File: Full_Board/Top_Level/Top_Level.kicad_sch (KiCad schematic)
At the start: 3 parts

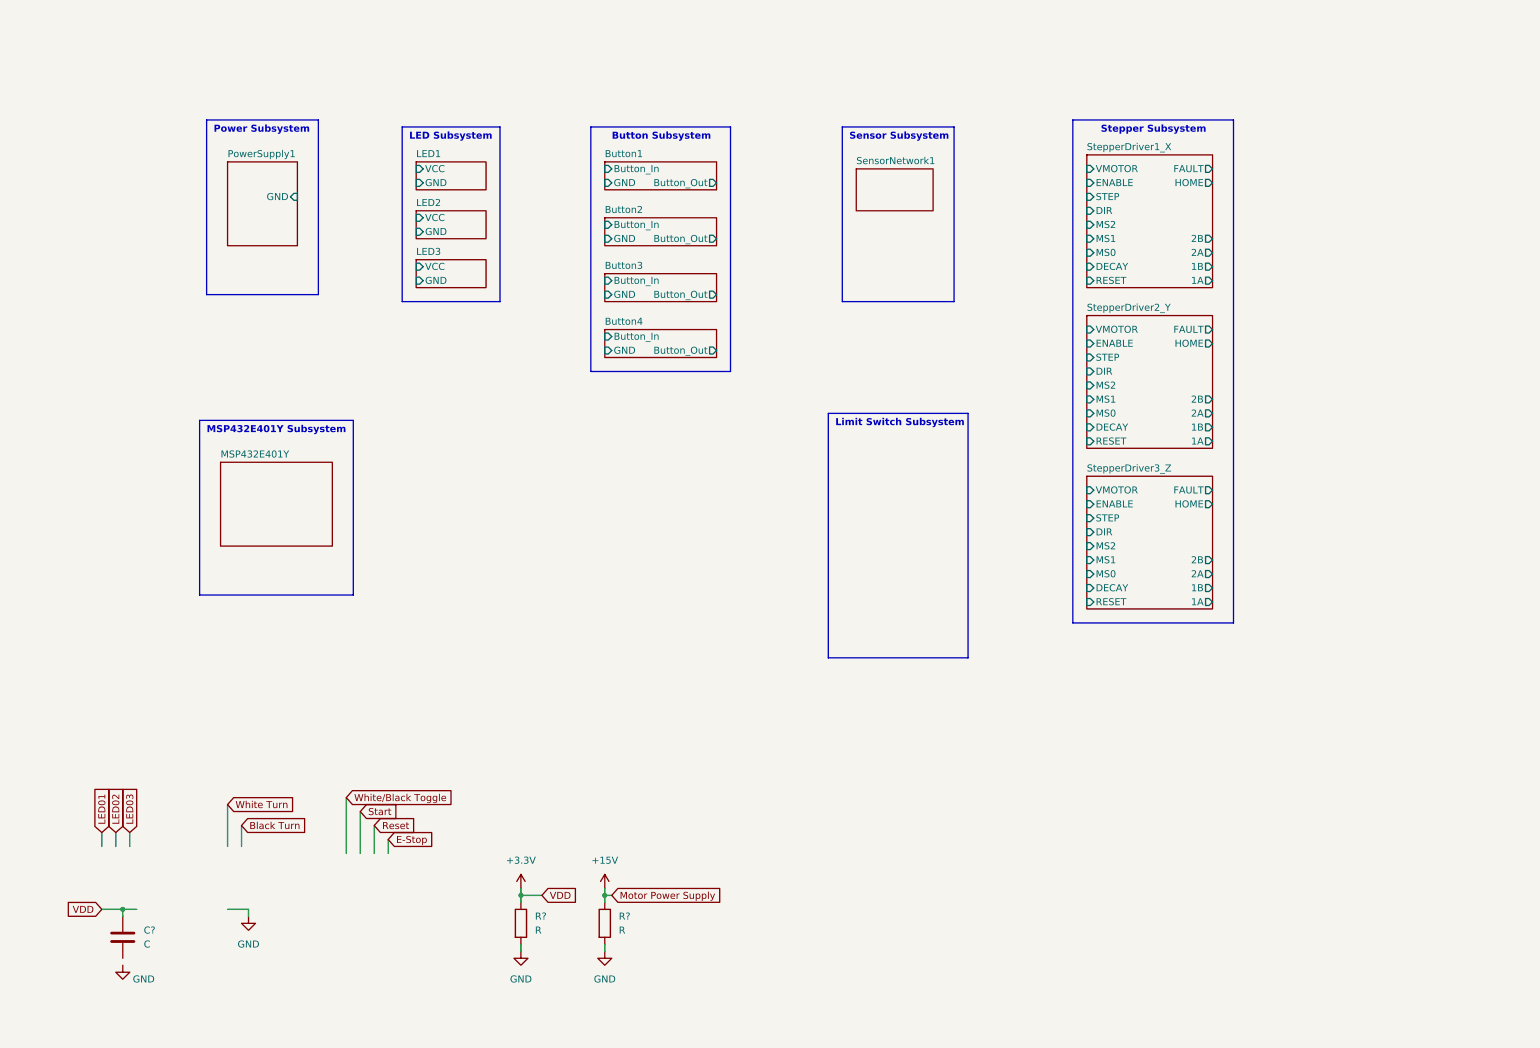
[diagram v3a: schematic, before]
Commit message: Finalize MSP432, stepper, and button subsheets
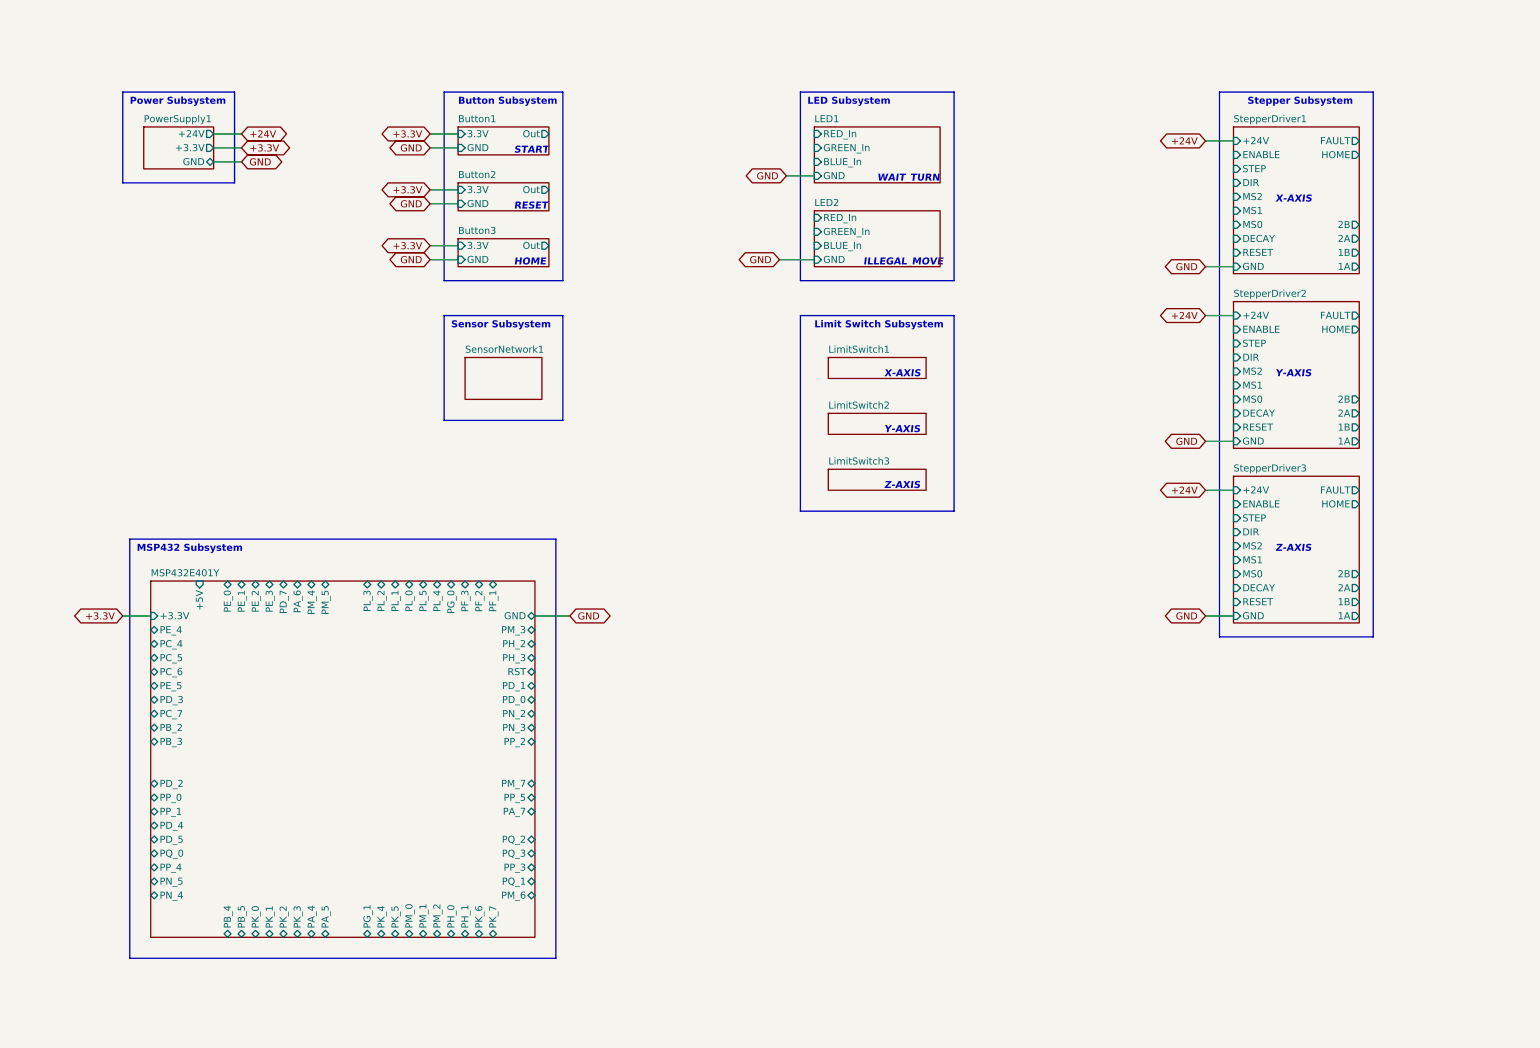
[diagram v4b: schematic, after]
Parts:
- removed C?: C, symbol Device:C
- removed R? (x2): R, symbol Device:R
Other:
- sheet StepperDriver1_X renamed StepperDriver1
- removed sheet Button4
- removed sheet LED3
- removed sheet StepperDriver2_Y
- removed sheet StepperDriver3_Z
- added sheet LimitSwitch1 (../Limit_Switch_Subsystem/LimitSwitch.kicad_sch)
- added sheet LimitSwitch2 (../Limit_Switch_Subsystem/LimitSwitch.kicad_sch)
- added sheet LimitSwitch3 (../Limit_Switch_Subsystem/LimitSwitch.kicad_sch)
- added sheet StepperDriver2 (../Stepper_Subsystem/Stepper_Driver.kicad_sch)
- added sheet StepperDriver3 (../Stepper_Subsystem/Stepper_Driver.kicad_sch)
- sheet Button1 ports: added 3.3V, Out; removed Button_In, Button_Out
- sheet Button2 ports: added 3.3V, Out; removed Button_In, Button_Out
- sheet Button3 ports: added 3.3V, Out; removed Button_In, Button_Out
- sheet LED1 ports: added BLUE_In, GREEN_In, RED_In; removed VCC
- sheet LED2 ports: added BLUE_In, GREEN_In, RED_In; removed VCC
- sheet MSP432E401Y ports: added +3.3V, +5V, GND, PA_4, PA_5, PA_6, PA_7, PB_2, PB_3, PB_4, PB_5, PC_4, PC_5, PC_6, PC_7, PD_0, PD_1, PD_2, PD_3, PD_4, PD_5, PD_7, PE_0, PE_1, PE_2, PE_3, PE_4, PE_5, PF_1, PF_2, PF_3, PG_0, PG_1, PH_0, PH_1, PH_2, PH_3, PK_0, PK_1, PK_2, PK_3, PK_4, PK_5, PK_6, PK_7, PL_0, PL_1, PL_2, PL_3, PL_4, PL_5, PM_0, PM_1, PM_2, PM_3, PM_4, PM_5, PM_6, PM_7, PN_2, PN_3, PN_4, PN_5, PP_0, PP_1, PP_2, PP_3, PP_4, PP_5, PQ_0, PQ_1, PQ_2, PQ_3, RST; removed none
- sheet PowerSupply1 ports: added +24V, +3.3V; removed none
- sheet StepperDriver1 ports: added +24V, GND; removed VMOTOR
- note added: "HOME"
- note added: "ILLEGAL_MOVE"
- note added: "MSP432 Subsystem"
- note added: "RESET"
- note added: "START"
- note added: "WAIT_TURN"
- note added: "X-AXIS"
- note added: "Y-AXIS"
- note added: "Z-AXIS"
- note removed: "MSP432E401Y Subsystem"

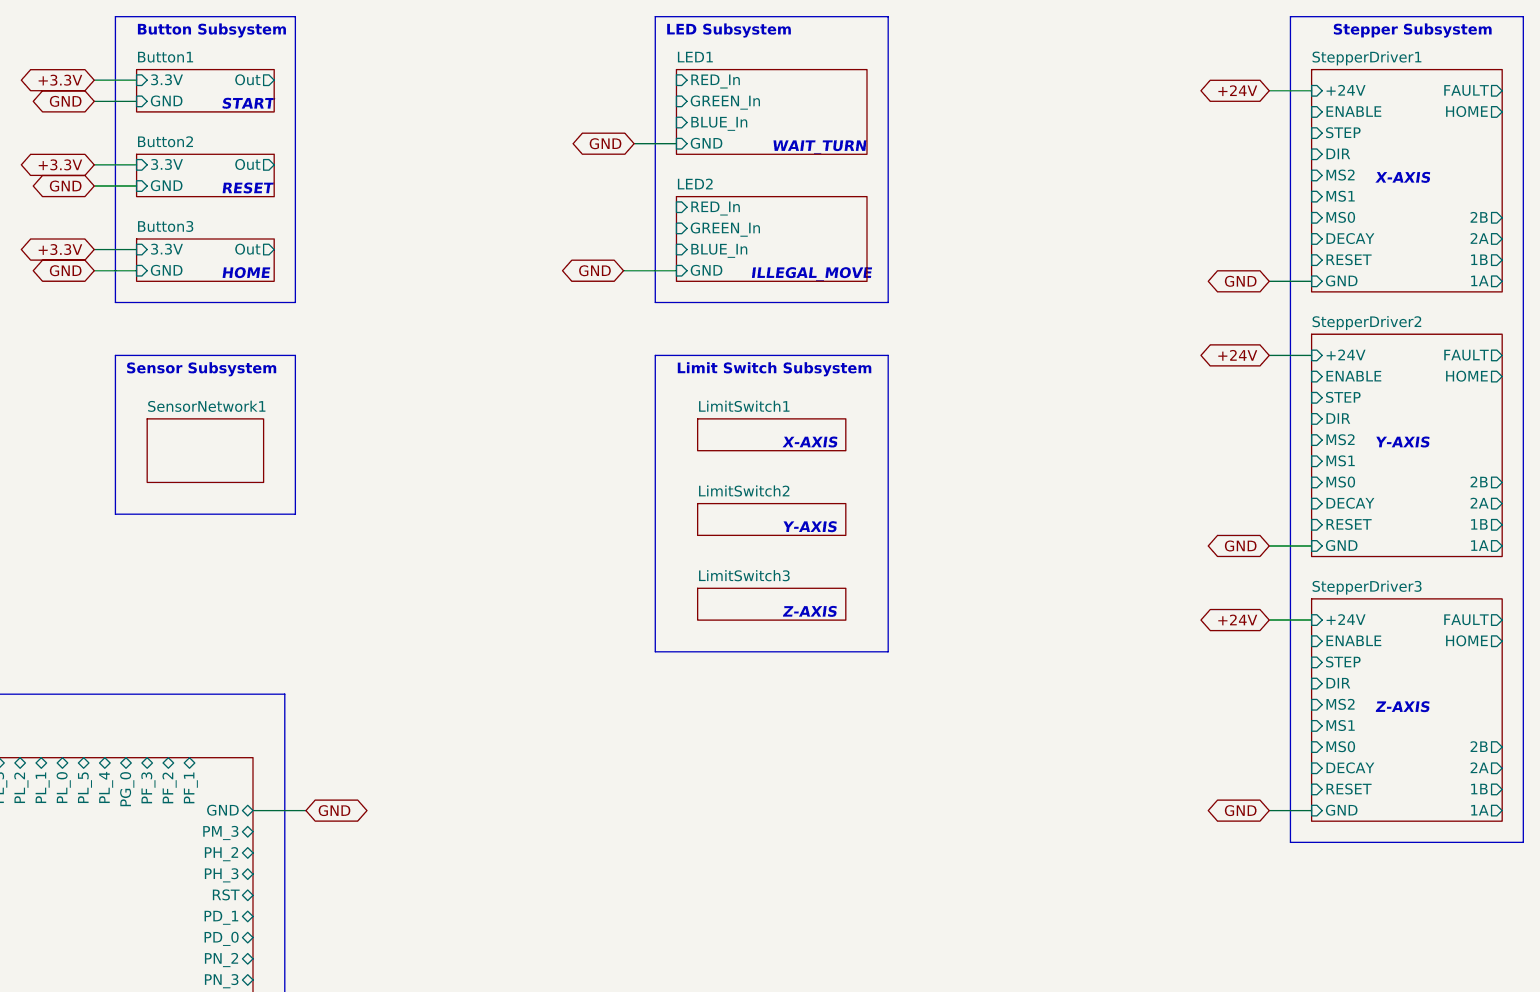
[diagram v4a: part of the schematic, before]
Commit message: Layout LED subsystem
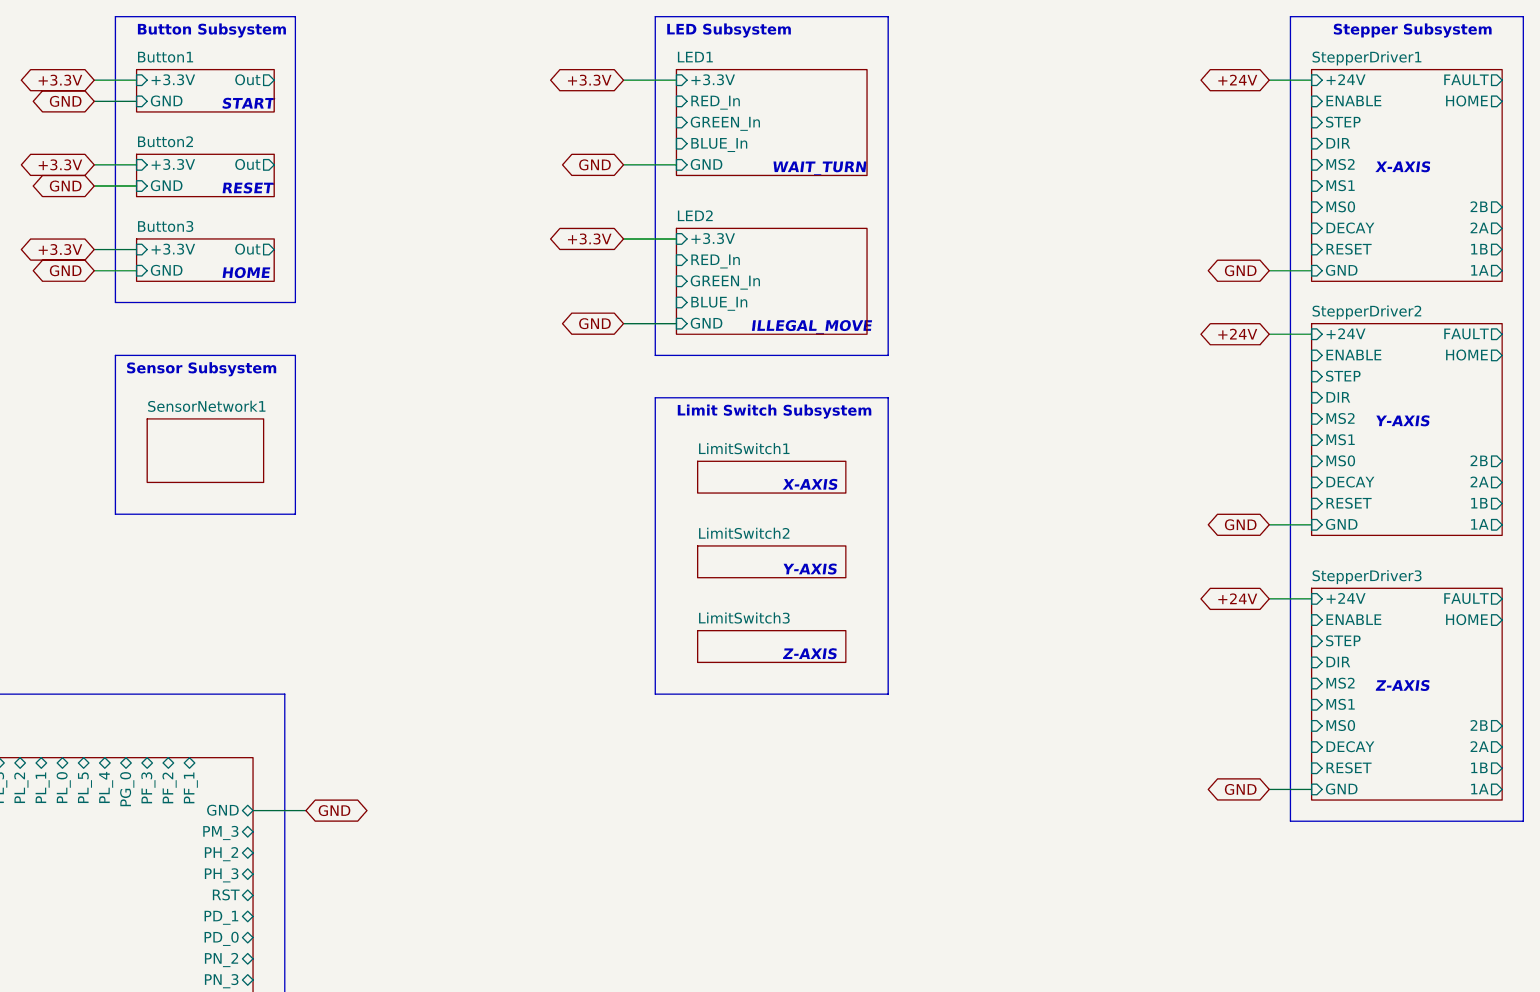
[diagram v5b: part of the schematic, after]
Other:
- sheet Button1 ports: added +3.3V; removed 3.3V
- sheet Button2 ports: added +3.3V; removed 3.3V
- sheet Button3 ports: added +3.3V; removed 3.3V
- sheet LED1 ports: added +3.3V; removed none
- sheet LED2 ports: added +3.3V; removed none
